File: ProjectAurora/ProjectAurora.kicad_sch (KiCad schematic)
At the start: 23 parts, among them J1 USB_C_Receptacle_USB2.0_14P, U1 STM32U031K8Ux, U2 CP2102N-Axx-xQFN20, U3 TPD2EUSB30A, Y1 ABS07-32.768KHZ-T

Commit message: Sensors and LEDs
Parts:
- removed C8: 100nF, symbol Device:C
- removed C9: 4.7nF, symbol Device:C
- removed J1: USB_C_Receptacle_USB2.0_14P, symbol Connector:USB_C_Receptacle_USB2.0_14P
- removed R3, R4: 5.1K, symbol Device:R
- removed R5: 10K, symbol Device:R
- removed R6: 22.1K, symbol Device:R
- removed R7: 47.5K, symbol Device:R
- removed R8: 1M, symbol Device:R
- removed TP1: TestPoint_2Pole, symbol Connector:TestPoint_2Pole
- removed U2: CP2102N-Axx-xQFN20, Package_DFN_QFN:SiliconLabs_QFN-20-1EP_3x3mm_P0.5mm_EP1.8x1.8mm, symbol Interface_USB:CP2102N-Axx-xQFN20
- removed U3: TPD2EUSB30A, Package_TO_SOT_SMD:Texas_DRT-3, symbol Power_Protection:TPD2EUSB30A
- added TP2: TestPoint_2Pole, symbol Connector:TestPoint_2Pole
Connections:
- net Charge-Fault: now also U1.9 (PA3); no longer U1.7 (PA1)
- net GND: now also TP2.2
- net Low-Power: now also U1.10 (PA4); no longer U1.8 (PA2)
- net NRST: now also TP2.1
- net TEMP_ALRT: now reaches U1.11 (PA5)
- net Wake-On-Raise renamed XL_INT_1
- new net MAG_INT: U1.8 (PA2)
- new net XL_INT_2: U1.7 (PA1)
- no-connect marks 20 -> 9
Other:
- added sheet LEDs & Controller (LED-Controller.kicad_sch)
- added sheet Sensors (sensors.kicad_sch)
- added sheet USB & Debug (usb-debug.kicad_sch)

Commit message: Schematic Done
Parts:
- added R19, R20: 10K, symbol Device:R
- added SW1, SW2: SW_Push, symbol Switch:SW_Push
- C3, C4: value 100nF -> 0.1uF
- C6: value 10nF -> 0.01uF
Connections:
- net +3V3: now also R19.1, R20.2
- net GND: now also SW1.1, SW2.2
- net Left-Button: now also U1.21 (PA11), R20.1, SW1.2; no longer U1.12 (PA6)
- net Right-Button: now also U1.22 (PA12), R19.2, SW2.1; no longer U1.13 (PA7)
- net TEMP_ALRT: no longer U1.11 (PA5)
- net Charge-Fault renamed CHARGE_STAT_1
- net Low-Power renamed CHARGE_STAT_2
- new net ~{CHARGE_EN}: U1.12 (PA6)
- new net ~{SOC_ALRT}: U1.11 (PA5)
- no-connect marks 9 -> 8
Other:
- added sheet Power & Battery (power-and-battery.kicad_sch)

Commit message: Starting Layout
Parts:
- removed SW1, SW2: SW_Push, symbol Switch:SW_Push
- added S1, S2: EVP-AA202K, EVP-AA202K:EVPAA202K, symbol EVP-AA202K:EVP-AA202K
- C1, C2, C3, C4, C5, C6, C7: footprint (none) -> Capacitor_SMD:C_0603_1608Metric
- R1, R19, R2, R20: footprint (none) -> Resistor_SMD:R_0603_1608Metric
- TP2: footprint (none) -> Test-Point-Jumper:2-Pin-Jumper; now not fitted
- Y1: footprint (none) -> ASCO:ABS07
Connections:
- net GND: now also S1.A2 (COM_1), S1.B2 (COM_2), S2.A2 (COM_1), S2.B2 (COM_2)
- net LED_SHUTDOWN: now also U1.31 (PF3); no longer U1.28 (PB5)
- net Left-Button: now also S2.A1 (NO_1), S2.B1 (NO_2)
- net Right-Button: now also S1.A1 (NO_1), S1.B1 (NO_2)
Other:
- moved on the sheet: R20

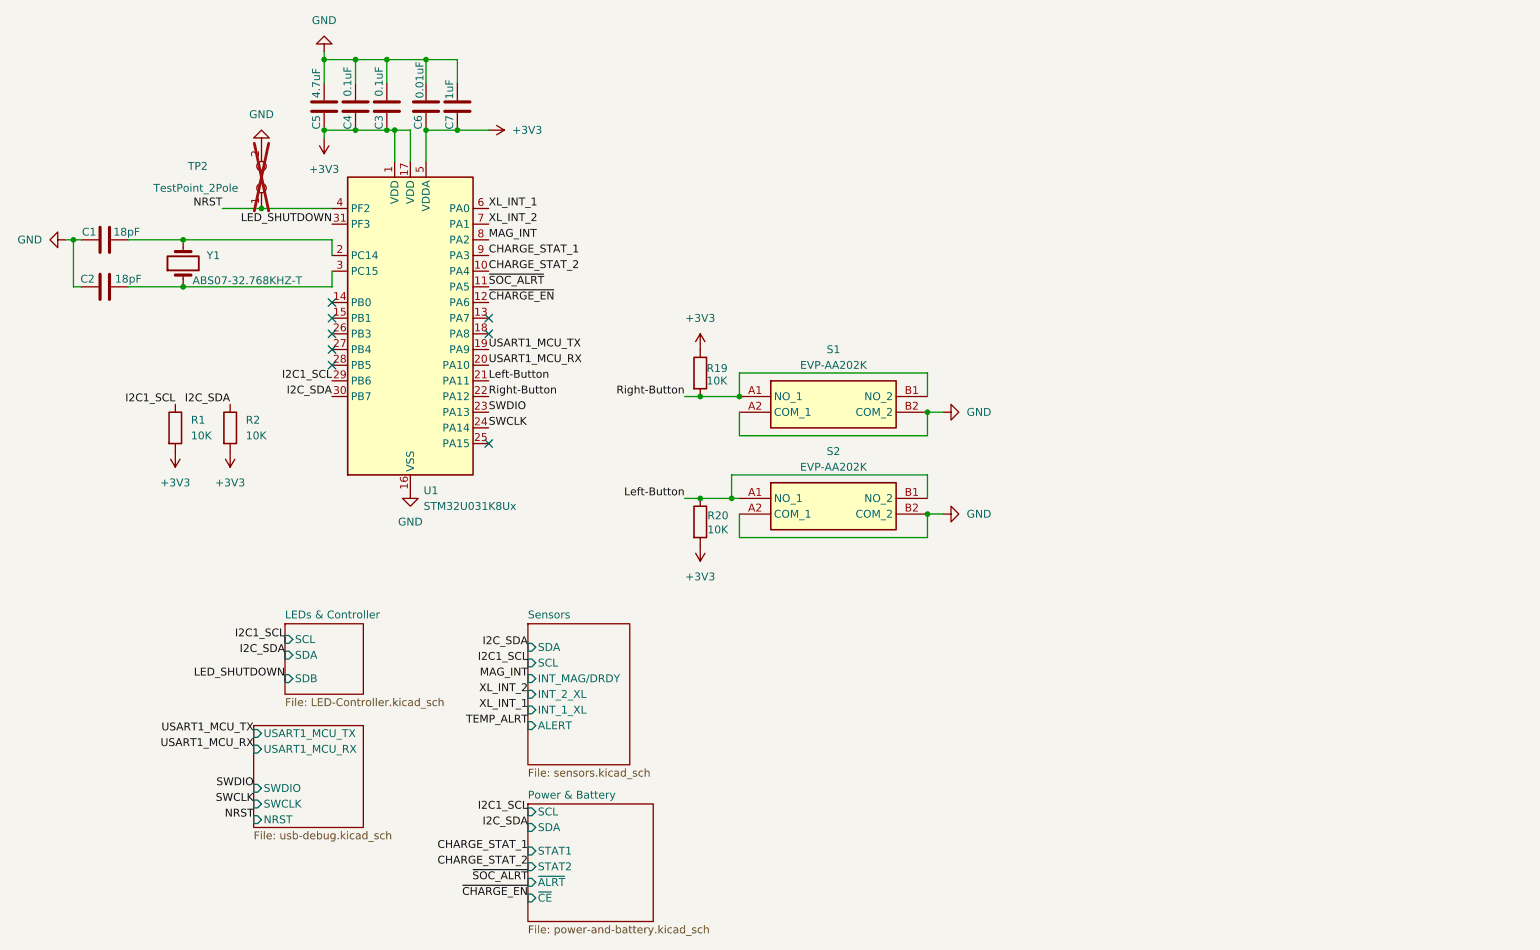
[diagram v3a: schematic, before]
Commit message: Prototype Board Layout Done
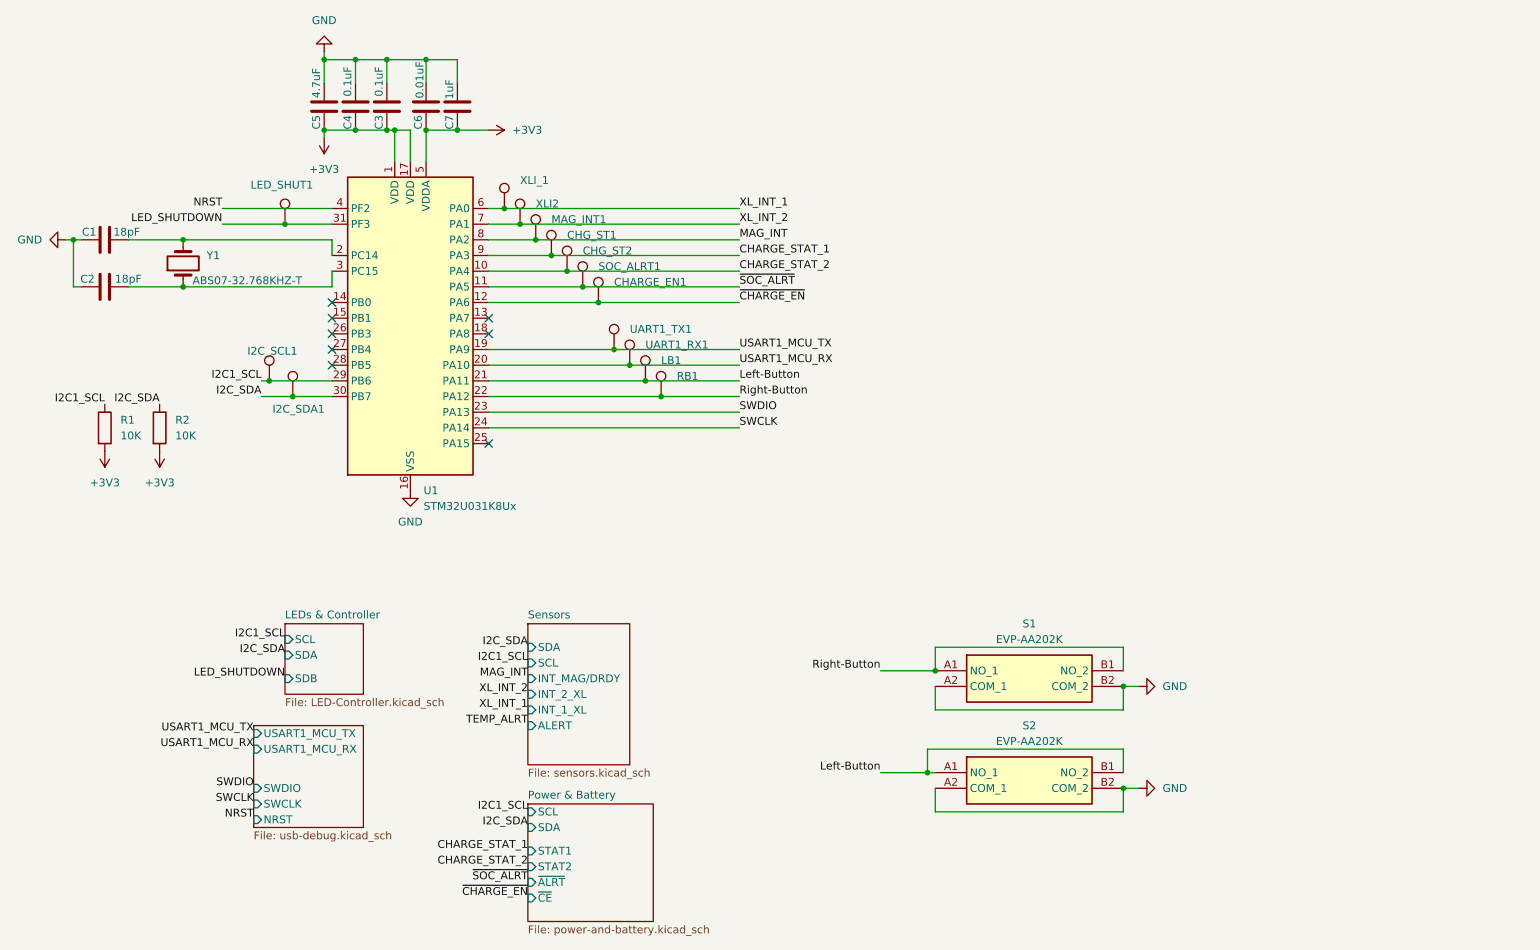
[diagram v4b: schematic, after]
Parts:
- removed R19, R20: 10K, Resistor_SMD:R_0603_1608Metric, symbol Device:R
- removed TP2: TestPoint_2Pole, Test-Point-Jumper:2-Pin-Jumper, symbol Connector:TestPoint_2Pole
- added CHARGE_EN1, CHG_ST1, CHG_ST2, I2C_SCL1, I2C_SDA1, LB1, LED_SHUT1, MAG_INT1, RB1, SOC_ALRT1, UART1_RX1, UART1_TX1, XLI2, XLI_1: TestPoint, TestPoint:TestPoint_Pad_1.0x1.0mm, symbol Connector:TestPoint
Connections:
- net CHARGE_STAT_1: now also CHG_ST1.1
- net CHARGE_STAT_2: now also CHG_ST2.1
- net I2C1_SCL: now also I2C_SCL1.1
- net I2C_SDA: now also I2C_SDA1.1
- net LED_SHUTDOWN: now also LED_SHUT1.1
- net Left-Button: now also LB1.1
- net MAG_INT: now also MAG_INT1.1
- net Right-Button: now also RB1.1
- net USART1_MCU_RX: now also UART1_RX1.1
- net USART1_MCU_TX: now also UART1_TX1.1
- net XL_INT_1: now also XLI_1.1
- net XL_INT_2: now also XLI2.1
- net ~{CHARGE_EN}: now also CHARGE_EN1.1
- net ~{SOC_ALRT}: now also SOC_ALRT1.1
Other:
- moved on the sheet: R1, R2, S1, S2
